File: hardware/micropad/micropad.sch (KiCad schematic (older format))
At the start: 29 parts, among them J2 Conn_ARM_JTAG_SWD_10, J3 USB_B_Micro, SW1 SW_SPST, SW2 SW_SPST, SW3 SW_SPST, U1 LD1117S33TR_SOT223, U2 STM32F042K6Ux, U3 APA102

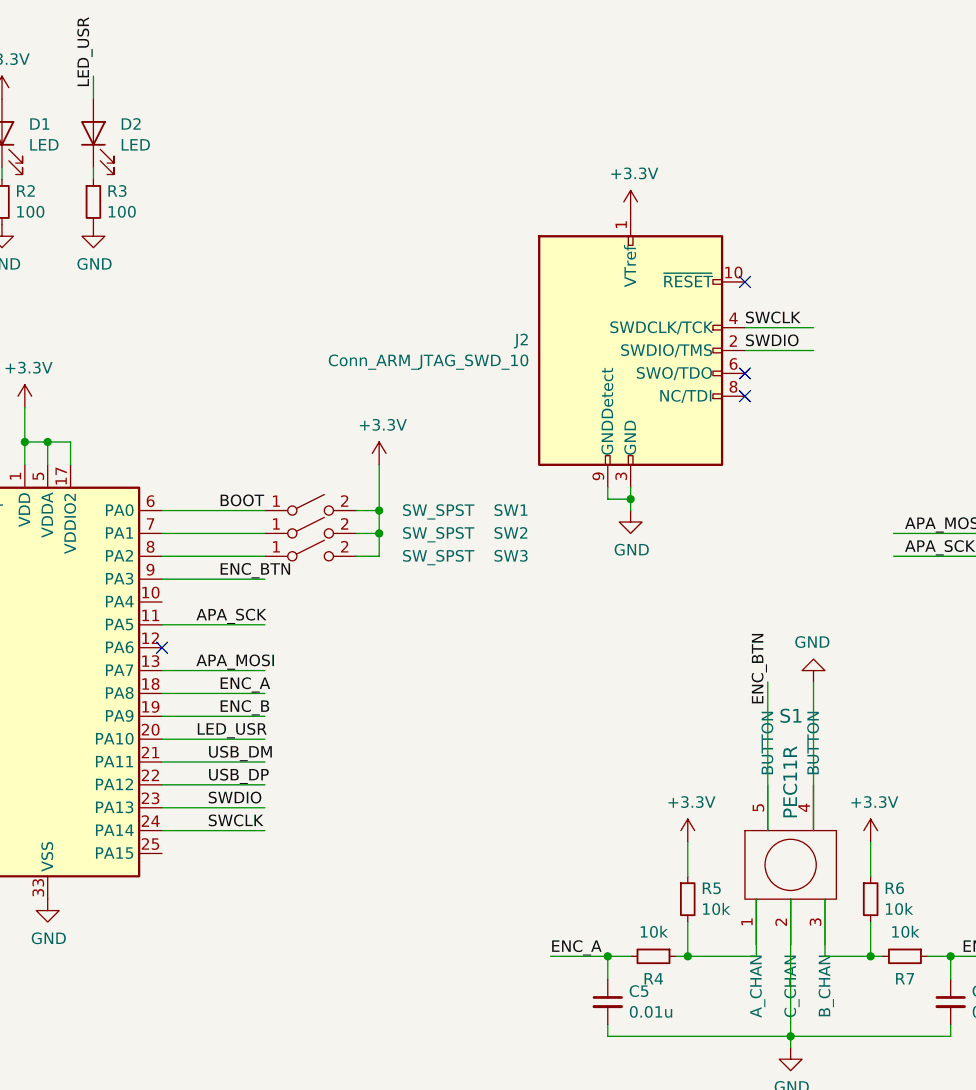
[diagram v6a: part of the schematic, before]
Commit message: Use temporary connector for SWD programming
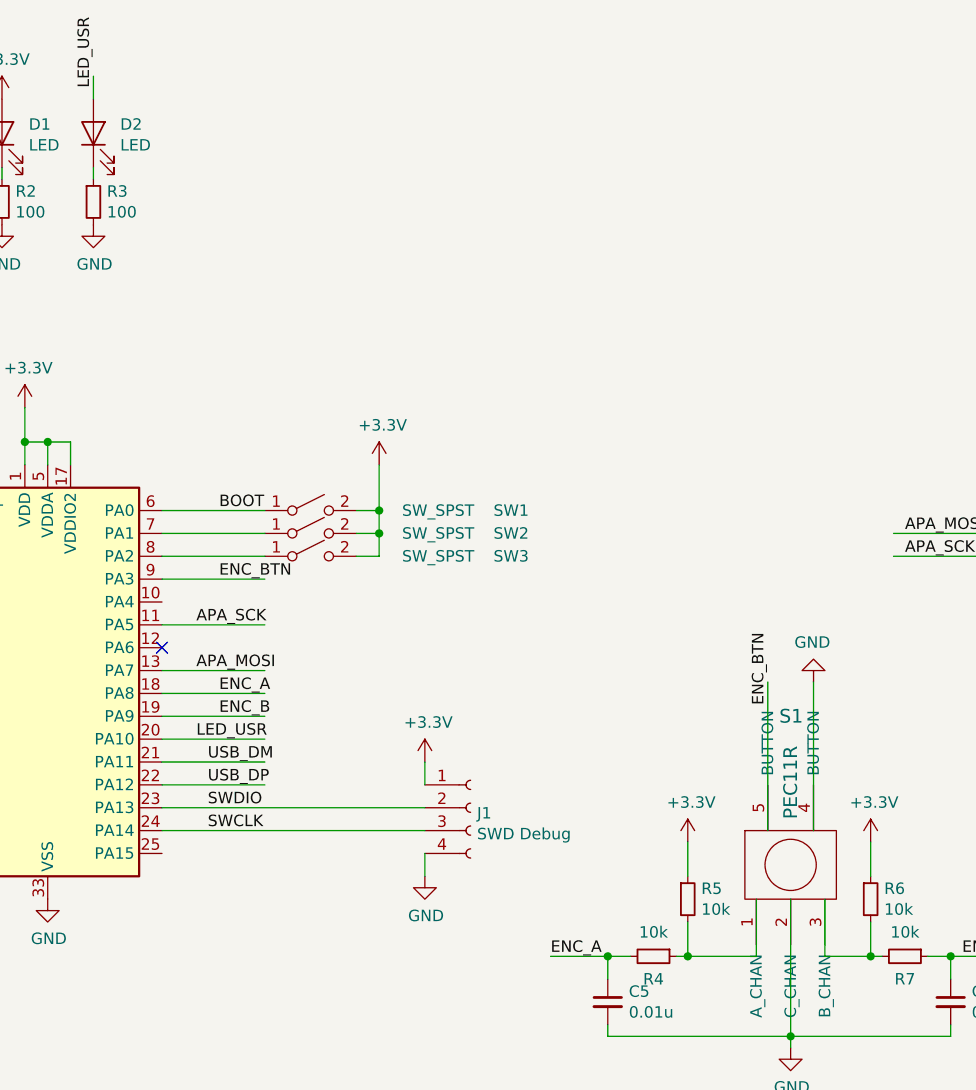
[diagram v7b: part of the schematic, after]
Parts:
- removed J2: Conn_ARM_JTAG_SWD_10, Pin_Headers:Pin_Header_Straight_2x05_Pitch1.27mm_SMD, symbol Connector:Conn_ARM_JTAG_SWD_10
- added J1: SWD Debug, micropad:REDFIT_IDC_SKEDD_CONN_4PIN, symbol Connector:Conn_01x04_Female
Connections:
- wire segments 83 -> 79
- no-connect marks 8 -> 5
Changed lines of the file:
@@
-$EndComp
-$Comp
-L Connector:Conn_ARM_JTAG_SWD_10 J2
-U 1 1 5FAE8451
-P 8200 2650
-F 0 "J2" H 7757 2696 50  0000 R CNN
-F 1 "Conn_ARM_JTAG_SWD_10" H 7757 2605 50  0000 R CNN
-F 2 "Pin_Headers:Pin_Header_Straight_2x05_Pitch1.27mm_SMD" H 8200 2650 50  0001 C CNN
-F 3 "http://infocenter.arm.com/help/topic/com.arm.doc.ddi0314h/DDI0314H_coresight_components_trm.pdf" V 7850 1400 50  0001 C CNN
-	1    8200 2650
-	1    0    0    -1
 $EndComp
 $Comp
@@
 Text Label 5850 1500 1    50   ~ 0
 LED_USR
-Wire Wire Line
-	6150 4650 6600 4650
 Text Label 6350 4650 0    50   ~ 0
 SWDIO
-Wire Wire Line
-	6150 4750 6600 4750
 Text Label 6350 4750 0    50   ~ 0
 SWCLK
-Wire Wire Line
-	9000 2550 8700 2550
-Text Label 8700 2550 0    50   ~ 0
-SWCLK
-Text Label 8700 2650 0    50   ~ 0
-SWDIO
-NoConn ~ 8700 2350
-Wire Wire Line
-	8700 2650 9000 2650
-Wire Wire Line
-	8200 3250 8200 3300
-$Comp
-L power:GND #PWR017
-U 1 1 5FB43000
-P 8200 3350
-F 0 "#PWR017" H 8200 3100 50  0001 C CNN
-F 1 "GND" H 8205 3177 50  0000 C CNN
-F 2 "" H 8200 3350 50  0001 C CNN
-F 3 "" H 8200 3350 50  0001 C CNN
-	1    8200 3350
-	1    0    0    -1
-$EndComp
-Wire Wire Line
-	8100 3250 8100 3300
-Wire Wire Line
-	8100 3300 8200 3300
-Connection ~ 8200 3300
-Wire Wire Line
-	8200 3300 8200 3350
-$Comp
-L power:+3.3V #PWR016
-U 1 1 5FB43E70
-P 8200 2050
-F 0 "#PWR016" H 8200 1900 50  0001 C CNN
-F 1 "+3.3V" H 8215 2223 50  0000 C CNN
-F 2 "" H 8200 2050 50  0001 C CNN
-F 3 "" H 8200 2050 50  0001 C CNN
-	1    8200 2050
-	1    0    0    -1
-$EndComp
-NoConn ~ 8700 2850
-NoConn ~ 8700 2750
 $Comp
 L Device:C_Small C1
@@
 Wire Wire Line
 	2200 3250 2200 3200
+$Comp
+L Connector:Conn_01x04_Female J1
+U 1 1 5FC001DB
+P 7500 4650
+F 0 "J1" H 7528 4626 50  0000 L CNN
+F 1 "SWD Debug" H 7528 4535 50  0000 L CNN
+F 2 "micropad:REDFIT_IDC_SKEDD_CONN_4PIN" H 7500 4650 50  0001 C CNN
+F 3 "~" H 7500 4650 50  0001 C CNN
+	1    7500 4650
+	1    0    0    -1
+$EndComp
+Wire Wire Line
+	7300 4550 7300 4450
+$Comp
+L power:+3.3V #PWR016
+U 1 1 5FC177A0
+P 7300 4450
+F 0 "#PWR016" H 7300 4300 50  0001 C CNN
+F 1 "+3.3V" H 7315 4623 50  0000 C CNN
+F 2 "" H 7300 4450 50  0001 C CNN
+F 3 "" H 7300 4450 50  0001 C CNN
+	1    7300 4450
+	1    0    0    -1
+$EndComp
+$Comp
+L power:GND #PWR017
+U 1 1 5FC17D03
+P 7300 4950
+F 0 "#PWR017" H 7300 4700 50  0001 C CNN
+F 1 "GND" H 7305 4777 50  0000 C CNN
+F 2 "" H 7300 4950 50  0001 C CNN
+F 3 "" H 7300 4950 50  0001 C CNN
+	1    7300 4950
+	1    0    0    -1
+$EndComp
+Wire Wire Line
+	7300 4850 7300 4950
+Wire Wire Line
+	6150 4650 7300 4650
+Wire Wire Line
+	6150 4750 7300 4750
 $EndSCHEMATC

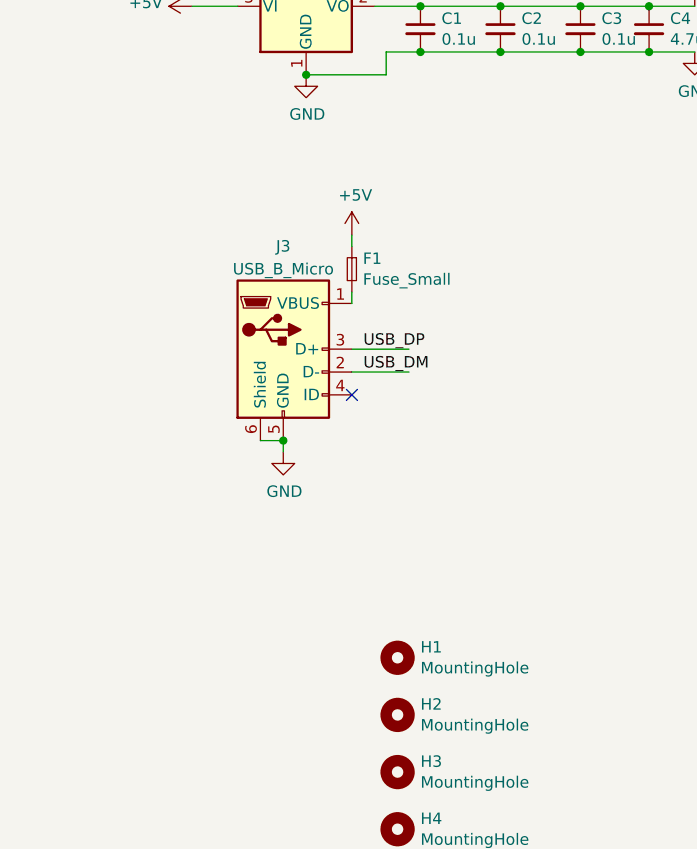
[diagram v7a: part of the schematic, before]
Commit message: Replace USB micro connector with USB-C connector
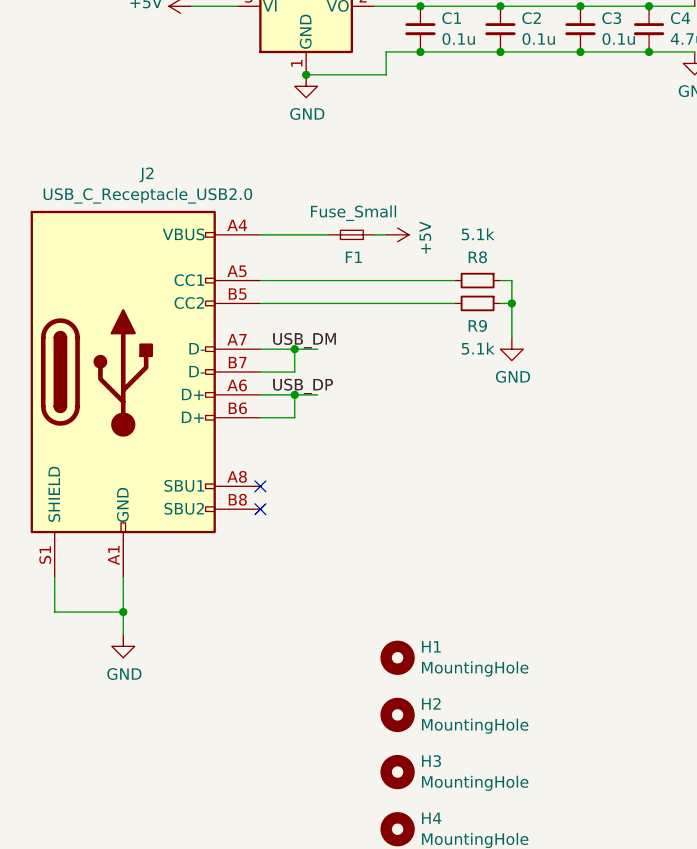
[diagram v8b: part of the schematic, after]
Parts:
- removed J3: USB_B_Micro, micropad:XKB-U254_USB, symbol Connector:USB_B_Micro
- added J2: USB_C_Receptacle_USB2.0, micropad:USB_C_Receptacle_Molex_1054500101, symbol Connector:USB_C_Receptacle_USB2.0
- added R8, R9: 5.1k, Resistors_SMD:R_0805, symbol Device:R_Small
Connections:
- wire segments 79 -> 93
- no-connect marks 5 -> 6
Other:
- moved on the sheet: F1
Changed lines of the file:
@@
 USB_DP
 Wire Wire Line
-	2200 3800 2450 3800
-Text Label 2250 3800 0    50   ~ 0
+	1800 3700 1950 3700
+Text Label 1850 3700 0    50   ~ 0
 USB_DM
 Wire Wire Line
-	2200 3700 2450 3700
-Text Label 2250 3700 0    50   ~ 0
+	1800 3900 1950 3900
+Text Label 1850 3900 0    50   ~ 0
 USB_DP
-$Comp
-L power:GND #PWR03
-U 1 1 5FAFFCA4
-P 1900 4150
-F 0 "#PWR03" H 1900 3900 50  0001 C CNN
-F 1 "GND" H 1905 3977 50  0000 C CNN
-F 2 "" H 1900 4150 50  0001 C CNN
-F 3 "" H 1900 4150 50  0001 C CNN
-	1    1900 4150
-	1    0    0    -1
-$EndComp
 $Comp
 L power:+5V #PWR04
 U 1 1 5FB029A9
-P 2200 3200
-F 0 "#PWR04" H 2200 3050 50  0001 C CNN
-F 1 "+5V" H 2215 3373 50  0000 C CNN
-F 2 "" H 2200 3200 50  0001 C CNN
-F 3 "" H 2200 3200 50  0001 C CNN
-	1    2200 3200
-	1    0    0    -1
+P 2350 3200
+F 0 "#PWR04" H 2350 3050 50  0001 C CNN
+F 1 "+5V" H 2365 3373 50  0000 C CNN
+F 2 "" H 2350 3200 50  0001 C CNN
+F 3 "" H 2350 3200 50  0001 C CNN
+	1    2350 3200
+	0    1    1    0
 $EndComp
 Wire Wire Line
@@
 Wire Wire Line
 	4650 3600 4650 3850
-Wire Wire Line
-	1900 4100 1900 4150
-Wire Wire Line
-	1800 4100 1900 4100
-NoConn ~ 2200 3900
 $Comp
 L apa102:APA102 U3
@@
 L Device:Fuse_Small F1
 U 1 1 5FB7A019
-P 2200 3350
-F 0 "F1" V 2154 3398 50  0000 L CNN
-F 1 "Fuse_Small" V 2245 3398 50  0000 L CNN
-F 2 "Capacitors_SMD:C_0603" H 2200 3350 50  0001 C CNN
-F 3 "~" H 2200 3350 50  0001 C CNN
-	1    2200 3350
-	0    1    1    0
-$EndComp
-Connection ~ 1900 4100
-$Comp
-L Connector:USB_B_Micro J3
-U 1 1 5FC27EEA
-P 1900 3700
-F 0 "J3" H 1900 4150 50  0000 C CNN
-F 1 "USB_B_Micro" H 1900 4050 50  0000 C CNN
-F 2 "micropad:XKB-U254_USB" H 2050 3650 50  0001 C CNN
-F 3 "~" H 2050 3650 50  0001 C CNN
-	1    1900 3700
-	1    0    0    -1
-$EndComp
-Wire Wire Line
-	2200 3500 2200 3450
-Wire Wire Line
-	2200 3250 2200 3200
+P 2200 3200
+F 0 "F1" H 2150 3300 50  0000 L CNN
+F 1 "Fuse_Small" H 2000 3100 50  0000 L CNN
+F 2 "Capacitors_SMD:C_0603" H 2200 3200 50  0001 C CNN
+F 3 "~" H 2200 3200 50  0001 C CNN
+	1    2200 3200
+	-1   0    0    1
+$EndComp
+Wire Wire Line
+	2300 3200 2350 3200
 $Comp
 L Connector:Conn_01x04_Female J1
@@
 Wire Wire Line
 	6150 4750 7300 4750
+Wire Wire Line
+	1800 3200 2100 3200
+Wire Wire Line
+	1800 3800 1950 3800
+Wire Wire Line
+	1950 3800 1950 3700
+Connection ~ 1950 3700
+Wire Wire Line
+	1950 3700 2050 3700
+Wire Wire Line
+	1800 4000 1950 4000
+Wire Wire Line
+	1950 4000 1950 3900
+Connection ~ 1950 3900
+Wire Wire Line
+	1950 3900 2050 3900
+Wire Wire Line
+	900  4700 900  4850
+Wire Wire Line
+	900  4850 1200 4850
+Wire Wire Line
+	1200 4850 1200 4700
+$Comp
+L power:GND #PWR0101
+U 1 1 5FE74BF5
+P 1200 4950
+F 0 "#PWR0101" H 1200 4700 50  0001 C CNN
+F 1 "GND" H 1205 4777 50  0000 C CNN
+F 2 "" H 1200 4950 50  0001 C CNN
+F 3 "" H 1200 4950 50  0001 C CNN
+	1    1200 4950
+	1    0    0    -1
+$EndComp
+Wire Wire Line
+	1200 4850 1200 4950
+Connection ~ 1200 4850
+$Comp
+L Device:R_Small R8
+U 1 1 5FE78123
+P 2750 3400
+F 0 "R8" V 2650 3400 50  0000 C CNN
+F 1 "5.1k" V 2550 3400 50  0000 C CNN
+F 2 "Resistors_SMD:R_0805" H 2750 3400 50  0001 C CNN
+F 3 "~" H 2750 3400 50  0001 C CNN
+	1    2750 3400
+	0    1    1    0
+$EndComp
+$Comp
+L Device:R_Small R9
+U 1 1 5FE790C5
+P 2750 3500
+F 0 "R9" V 2850 3500 50  0000 C CNN
+F 1 "5.1k" V 2950 3500 50  0000 C CNN
+F 2 "Resistors_SMD:R_0805" H 2750 3500 50  0001 C CNN
+F 3 "~" H 2750 3500 50  0001 C CNN
+	1    2750 3500
+	0    1    1    0
+$EndComp
+Wire Wire Line
+	1800 3400 2650 3400
+Wire Wire Line
+	1800 3500 2650 3500
+Wire Wire Line
+	2850 3400 2900 3400
+Wire Wire Line
+	2900 3400 2900 3500
+$Comp
+L power:GND #PWR0102
+U 1 1 5FE87C89
+P 2900 3650
+F 0 "#PWR0102" H 2900 3400 50  0001 C CNN
+F 1 "GND" H 2905 3477 50  0000 C CNN
+F 2 "" H 2900 3650 50  0001 C CNN
+F 3 "" H 2900 3650 50  0001 C CNN
+	1    2900 3650
+	1    0    0    -1
+$EndComp
+Wire Wire Line
+	2850 3500 2900 3500
+Connection ~ 2900 3500
+Wire Wire Line
+	2900 3500 2900 3650
+$Comp
+L Connector:USB_C_Receptacle_USB2.0 J2
+U 1 1 5FE4F0B9
+P 1200 3800
+F 0 "J2" H 1307 4667 50  0000 C CNN
+F 1 "USB_C_Receptacle_USB2.0" H 1307 4576 50  0000 C CNN
+F 2 "micropad:USB_C_Receptacle_Molex_1054500101" H 1350 3800 50  0001 C CNN
+F 3 "https://www.usb.org/sites/default/files/documents/usb_type-c.zip" H 1350 3800 50  0001 C CNN
+	1    1200 3800
+	1    0    0    -1
+$EndComp
+NoConn ~ 1800 4300
+NoConn ~ 1800 4400
 $EndSCHEMATC
